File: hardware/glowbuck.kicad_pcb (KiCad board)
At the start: 4 copper layers, 80 x 50 mm, 132 parts, among them J101 Conn_02x08_Odd_Even, J102 Conn_01x04_Socket, J103 Conn_01x01_Pin, J104 Conn_01x01_Pin, J105 Conn_01x01_Pin, J106 Conn_01x01_Pin, J201 USB_C_Receptacle_USB2.0_16P, J202 USB_C_Receptacle_USB2.0_16P, Q401 2N7002NXAKR, SW101 SW_Push, SW102 SW_Push, U101 ESP32-S3-WROOM-1, U102 INA181A3, U103 SN74LVC1T45DBV, U201 TPS25730D, U202 TPD2E2U06DCK, U301 AP63203WU, U401 SIC437A

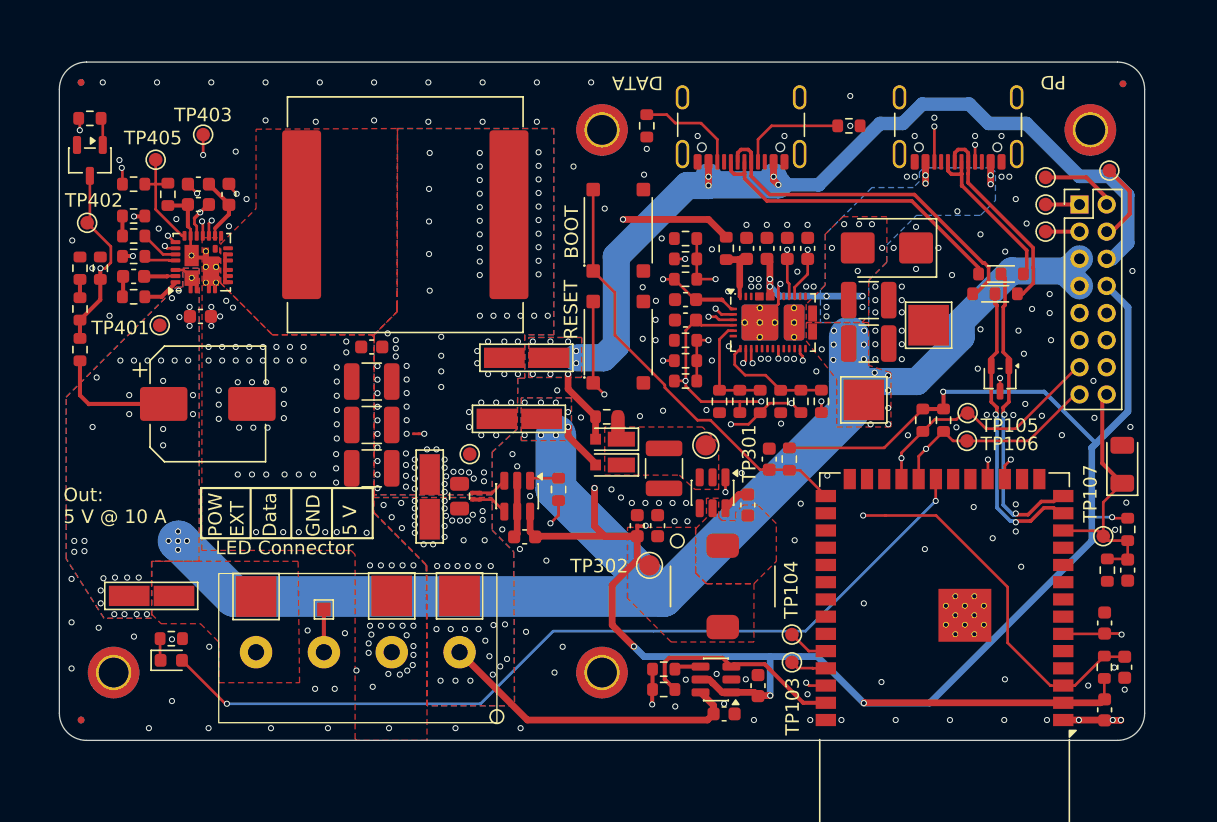
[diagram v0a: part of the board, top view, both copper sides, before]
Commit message: Thermal reliefes
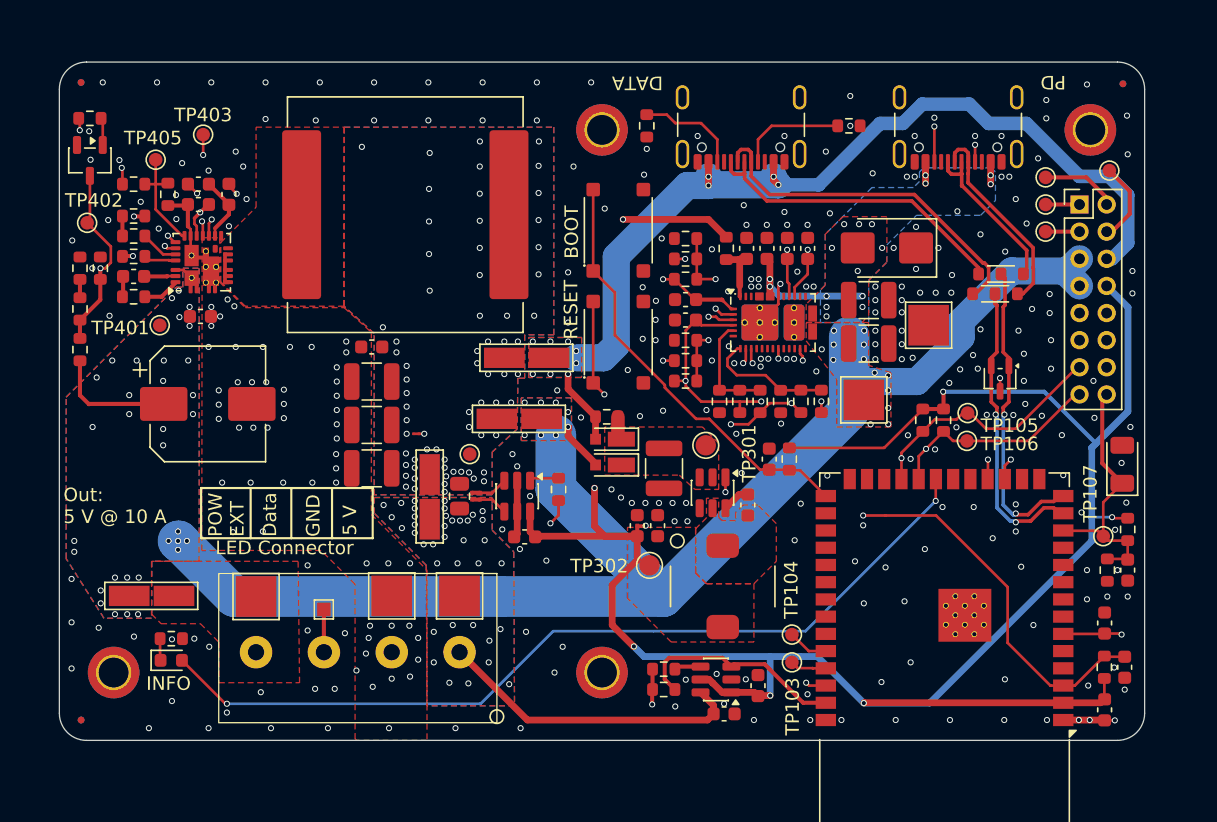
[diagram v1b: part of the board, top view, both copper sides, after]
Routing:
- net /USB-C and PD/PD_ADC4: track 8.53 -> 9.47 mm
- net GND: track 16.9 -> 16.5 mm, vias 269 -> 300
- net VBUS: vias 60 -> 54
- net VOUT: vias 91 -> 66
- net /LED_POW: vias 44 -> 38
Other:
- board text added: "INFO"

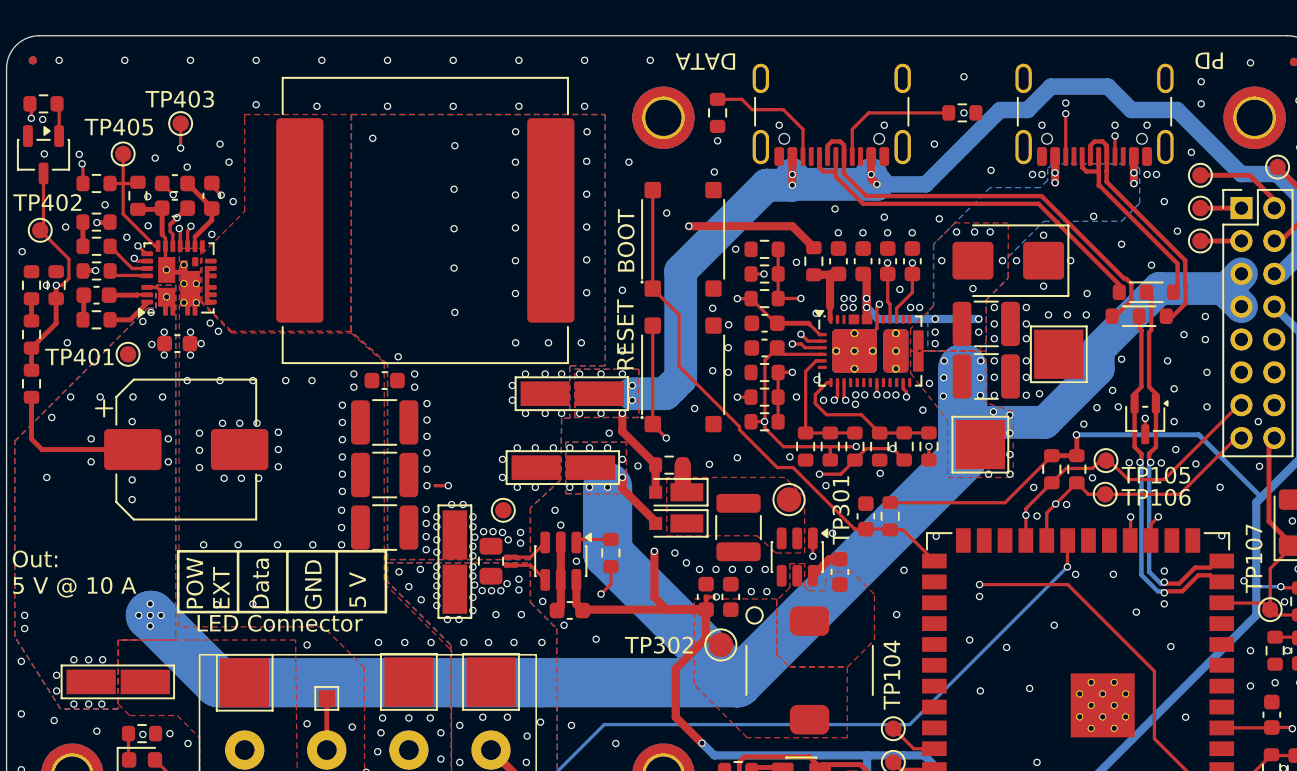
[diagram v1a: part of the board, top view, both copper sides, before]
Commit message: Exchanged 5k11 with 5k1 part number
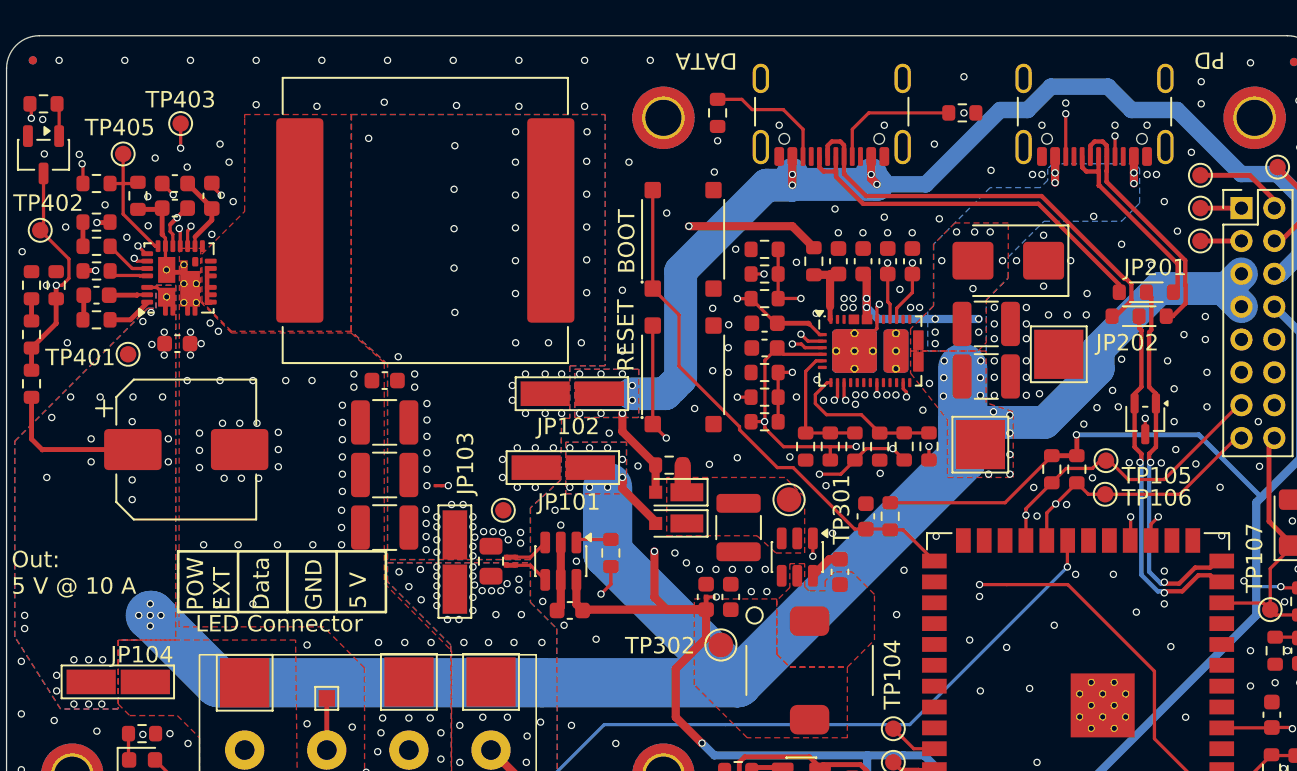
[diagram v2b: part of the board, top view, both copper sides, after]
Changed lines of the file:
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@@
 			)
 		)
-		(property "MouserNumber" "603-RT0603DRE075K11L"
+		(property "MouserNumber" "603-RC0603FR-105K1L"
 			(at 0 0 270)
 			(unlocked yes)
@@
 			)
 		)
-		(property "ManufacturerNumber" "RT0603DRE075K11L"
+		(property "ManufacturerNumber" "RC0603FR-105K1L"
 			(at 0 0 270)
 			(unlocked yes)
@@
 		(tags "net tie solder jumper bridged")
 		(property "Reference" "JP104"
-			(at 0 -1.8 0)
+			(at -1.45 1.65 0)
 			(layer "F.SilkS")
-			(hide yes)
 			(effects
 				(font
 					(size 1 1)
-					(thickness 0.15)
+					(thickness 0.153)
 				)
 			)
@@
 			)
 		)
-		(property "MouserNumber" "603-RT0603DRE075K11L"
+		(property "MouserNumber" "603-RC0603FR-105K1L"
 			(at 0 0 270)
 			(unlocked yes)
@@
 			)
 		)
-		(property "ManufacturerNumber" "RT0603DRE075K11L"
+		(property "ManufacturerNumber" "RC0603FR-105K1L"
 			(at 0 0 270)
 			(unlocked yes)
@@
 			)
 		)
-		(property "MouserNumber" "603-RT0603DRE075K11L"
+		(property "MouserNumber" "603-RC0603FR-105K1L"
 			(at 0 0 270)
 			(unlocked yes)
@@
 			)
 		)
-		(property "ManufacturerNumber" "RT0603DRE075K11L"
+		(property "ManufacturerNumber" "RC0603FR-105K1L"
 			(at 0 0 270)
 			(unlocked yes)
@@
 			)
 		)
-		(property "MouserNumber" "603-RT0603DRE075K11L"
+		(property "MouserNumber" "603-RC0603FR-105K1L"
 			(at 0 0 270)
 			(unlocked yes)
@@
 			)
 		)
-		(property "ManufacturerNumber" "RT0603DRE075K11L"
+		(property "ManufacturerNumber" "RC0603FR-105K1L"
 			(at 0 0 270)
 			(unlocked yes)
@@
 				(font
 					(size 1 1)
-					(thickness 0.15)
+					(thickness 0.153)
 				)
 			)
@@
 			(at -0.72 1.62 0)
 			(layer "F.SilkS")
-			(hide yes)
 			(effects
 				(font
@@
 			)
 		)
-		(property "MouserNumber" "603-RT0603DRE075K11L"
+		(property "MouserNumber" "603-RC0603FR-105K1L"
 			(at 0 0 90)
 			(unlocked yes)
@@
 			)
 		)
-		(property "ManufacturerNumber" "RT0603DRE075K11L"
+		(property "ManufacturerNumber" "RC0603FR-105K1L"
 			(at 0 0 90)
 			(unlocked yes)
@@
 			)
 		)
-		(property "MouserNumber" "603-RT0603DRE075K11L"
+		(property "MouserNumber" "603-RC0603FR-105K1L"
 			(at 0 0 270)
 			(unlocked yes)
@@
 			)
 		)
-		(property "ManufacturerNumber" "RT0603DRE075K11L"
+		(property "ManufacturerNumber" "RC0603FR-105K1L"
 			(at 0 0 270)
 			(unlocked yes)
@@
 			)
 		)
-		(property "MouserNumber" "603-RT0603DRE075K11L"
+		(property "MouserNumber" "603-RC0603FR-105K1L"
 			(at 0 0 0)
 			(unlocked yes)
@@
 			)
 		)
-		(property "ManufacturerNumber" "RT0603DRE075K11L"
+		(property "ManufacturerNumber" "RC0603FR-105K1L"
 			(at 0 0 0)
 			(unlocked yes)
@@
 			)
 		)
-		(property "MouserNumber" "603-RT0603DRE075K11L"
+		(property "MouserNumber" "603-RC0603FR-105K1L"
 			(at 0 0 180)
 			(unlocked yes)
@@
 			)
 		)
-		(property "ManufacturerNumber" "RT0603DRE075K11L"
+		(property "ManufacturerNumber" "RC0603FR-105K1L"
 			(at 0 0 180)
 			(unlocked yes)
@@
 			)
 		)
-		(property "MouserNumber" "603-RT0603DRE075K11L"
+		(property "MouserNumber" "603-RC0603FR-105K1L"
 			(at 0 0 270)
 			(unlocked yes)
@@
 			)
 		)
-		(property "ManufacturerNumber" "RT0603DRE075K11L"
+		(property "ManufacturerNumber" "RC0603FR-105K1L"
 			(at 0 0 270)
 			(unlocked yes)
@@
 			(at 0.54 -1.5 0)
 			(layer "F.SilkS")
-			(hide yes)
 			(effects
 				(font
@@
 			)
 		)
-		(property "MouserNumber" "603-RT0603DRE075K11L"
+		(property "MouserNumber" "603-RC0603FR-105K1L"
 			(at 0 0 90)
 			(unlocked yes)
@@
 			)
 		)
-		(property "ManufacturerNumber" "RT0603DRE075K11L"
+		(property "ManufacturerNumber" "RC0603FR-105K1L"
 			(at 0 0 90)
 			(unlocked yes)
@@
 		(tags "net tie solder jumper bridged")
 		(property "Reference" "JP103"
-			(at 0 -1.8 90)
+			(at 6 0.65 270)
 			(layer "F.SilkS")
-			(hide yes)
 			(effects
 				(font
@@
 			)
 		)
-		(property "Description" "Generic connector, single row, 01x04, script generated"
+		(property "Description" ""
 			(at 0 0 270)
 			(unlocked yes)
@@
 			)
 		)
-		(property "MouserNumber" "603-RT0603DRE075K11L"
+		(property "MouserNumber" "603-RC0603FR-105K1L"
 			(at 0 0 0)
 			(unlocked yes)
@@
 			)
 		)
-		(property "ManufacturerNumber" "RT0603DRE075K11L"
+		(property "ManufacturerNumber" "RC0603FR-105K1L"
 			(at 0 0 0)
 			(unlocked yes)
@@
 			)
 		)
-		(property "MouserNumber" "603-RT0603DRE075K11L"
+		(property "MouserNumber" "603-RC0603FR-105K1L"
 			(at 0 0 0)
 			(unlocked yes)
@@
 			)
 		)
-		(property "ManufacturerNumber" "RT0603DRE075K11L"
+		(property "ManufacturerNumber" "RC0603FR-105K1L"
 			(at 0 0 0)
 			(unlocked yes)
@@
 		(tags "net tie solder jumper bridged")
 		(property "Reference" "JP101"
-			(at -0.8 -2 0)
+			(at -0.35 -2.1 0)
 			(layer "F.SilkS")
-			(hide yes)
 			(effects
 				(font
@@
 		(tags "net tie solder jumper bridged")
 		(property "Reference" "JP102"
-			(at 0 -1.8 0)
+			(at 0.25 -2 0)
 			(layer "F.SilkS")
-			(hide yes)
 			(effects
 				(font
@@
 	)
 	(gr_rect
-		(start 78.05 59.45)
-		(end 83.05 64.45)
+		(start 74.15 60.45)
+		(end 79.15 65.45)
 		(stroke
 			(width 0.16)
@@
 			(font
 				(size 1 1)
-				(thickness 0.16)
+				(thickness 0.153)
 			)
 			(justify left top mirror)
@@
 	)
 	(via
-		(at 76.3 56.25)
+		(at 76.05 56.25)
 		(size 0.45)
 		(drill 0.3)
@@
 	)
 	(via
-		(at 81.2 54.3)
+		(at 81.4 54.25)
 		(size 0.45)
 		(drill 0.3)
@@
 	)
 	(via
-		(at 77.2 54.3)
+		(at 77 54.05)
 		(size 0.45)
 		(drill 0.3)
@@
 	)
 	(group ""
-		(members "88114caa-589f-49c8-b551-27622386bc59" "a1ba442d-18c4-4084-8eef-3d083ad60422")
-	)
-	(group ""
-		(members "84027013-9bce-432e-9a82-80b846cc659b" "df41fbdb-ae57-4a8d-a916-b01a02a27ec6")
-	)
-	(group ""

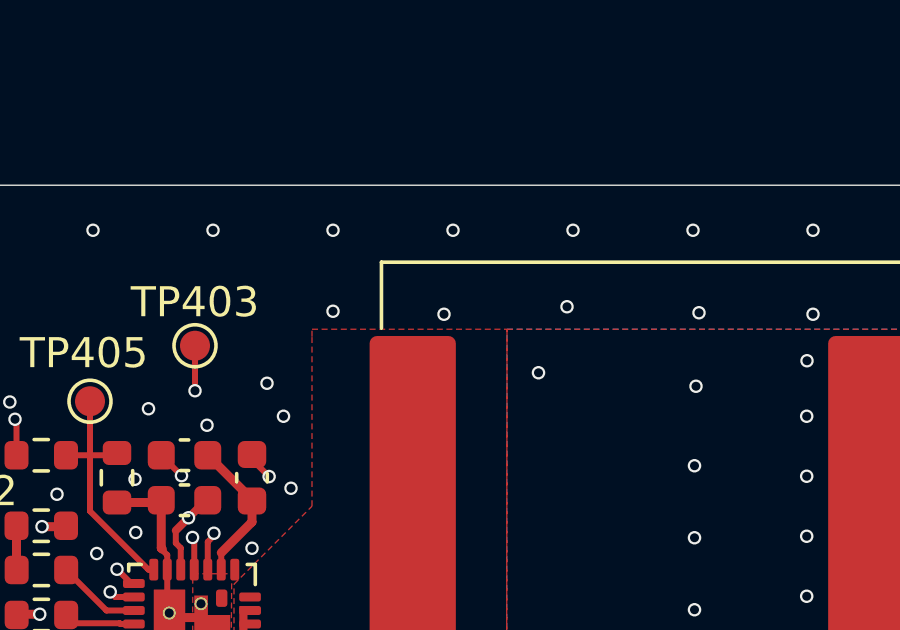
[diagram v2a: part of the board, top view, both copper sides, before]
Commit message: Adjusted product numbers and silkscreen for ordernumber
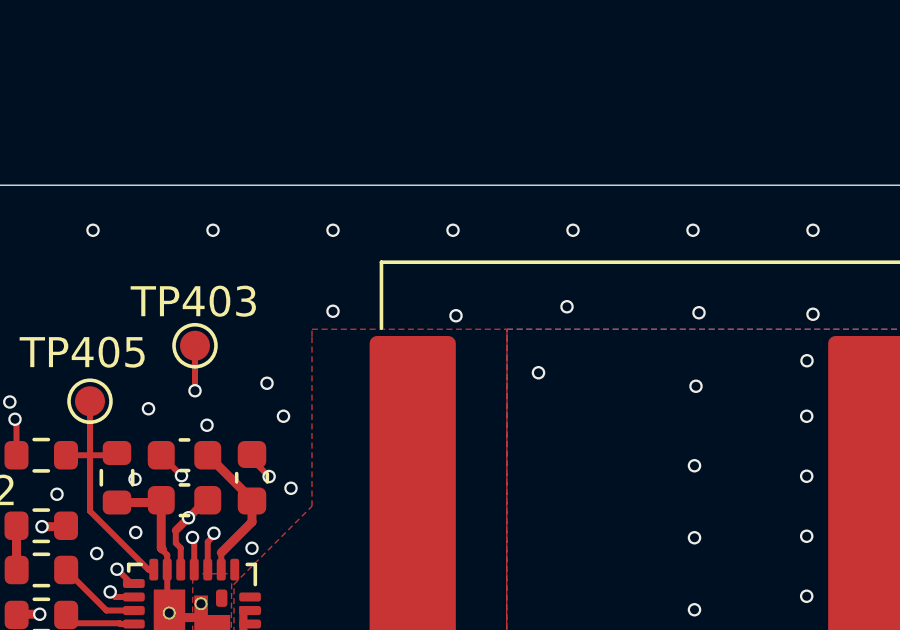
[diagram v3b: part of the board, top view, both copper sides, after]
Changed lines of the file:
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@@
 			)
 		)
-		(property "Datasheet" "~"
+		(property "Datasheet" "https://www.ckswitches.com/media/2780/pts526.pdf"
 			(at -0.2 -6.3 90)
 			(unlocked yes)
@@
 			)
 		)
-		(property "MouserNumber" "611-PTS526SM15SMTR2L"
+		(property "MouserNumber" "611-PTS526SM20S21LFS"
 			(at 0 0 90)
 			(unlocked yes)
@@
 			)
 		)
-		(property "ManufacturerNumber" "PTS526SM15SMTR2 LFS"
+		(property "ManufacturerNumber" "PTS526SM20SMTR21 LFS"
 			(at 0 0 90)
 			(unlocked yes)
@@
 			)
 		)
-		(property "Datasheet" "~"
+		(property "Datasheet" "https://www.ckswitches.com/media/2780/pts526.pdf"
 			(at -0.2 -6.3 90)
 			(unlocked yes)
@@
 			)
 		)
-		(property "MouserNumber" "611-PTS526SM15SMTR2L"
+		(property "MouserNumber" "611-PTS526SM20S21LFS"
 			(at 0 0 90)
 			(unlocked yes)
@@
 			)
 		)
-		(property "ManufacturerNumber" "PTS526SM15SMTR2 LFS"
+		(property "ManufacturerNumber" "PTS526SM20SMTR21 LFS"
 			(at 0 0 90)
 			(unlocked yes)
@@
 		(sheetname "/")
 		(sheetfile "glowbuck.kicad_sch")
-		(attr through_hole)
+		(attr through_hole exclude_from_bom)
 		(fp_line
 			(start -1.11 -1.11)
@@
 	)
 	(gr_rect
-		(start 74.15 60.45)
-		(end 79.15 65.45)
+		(start 69.1 60)
+		(end 79.1 62)
 		(stroke
 			(width 0.16)
@@
 	)
 	(via
-		(at 72.9 54.3)
+		(at 73.3 54.35)
 		(size 0.45)
 		(drill 0.3)
